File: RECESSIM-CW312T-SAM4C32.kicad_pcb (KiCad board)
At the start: 2 copper layers, 58.7 x 48.7 mm, 33 parts, among them U1 ATSAM4C32C

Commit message: Added two necessary resistors and removed one unnecessary one
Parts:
- added R6: 100k, Resistor_SMD:R_0603_1608Metric, F.Cu at (142.5, 102.2)
- R1: value 10k -> 100k
- moved R1 6.11 mm to (142.5, 104.2)
- moved R3 3.50 mm to (158.5, 89.3)
- moved TP2 3.20 mm to (143.8, 116.0)
- moved TP7 3.20 mm to (146.0, 116.0)
- moved R5 1.68 mm to (173.2, 109.8)
- moved C8 1.50 mm to (151.8, 116.8)
- moved C9 1.50 mm to (151.8, 118.5)
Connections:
- R1 pad 1: GND -> VCC
- R1 pad 2: Net-(JP1-C) -> Net-(U1-WKUP0/TMP0)

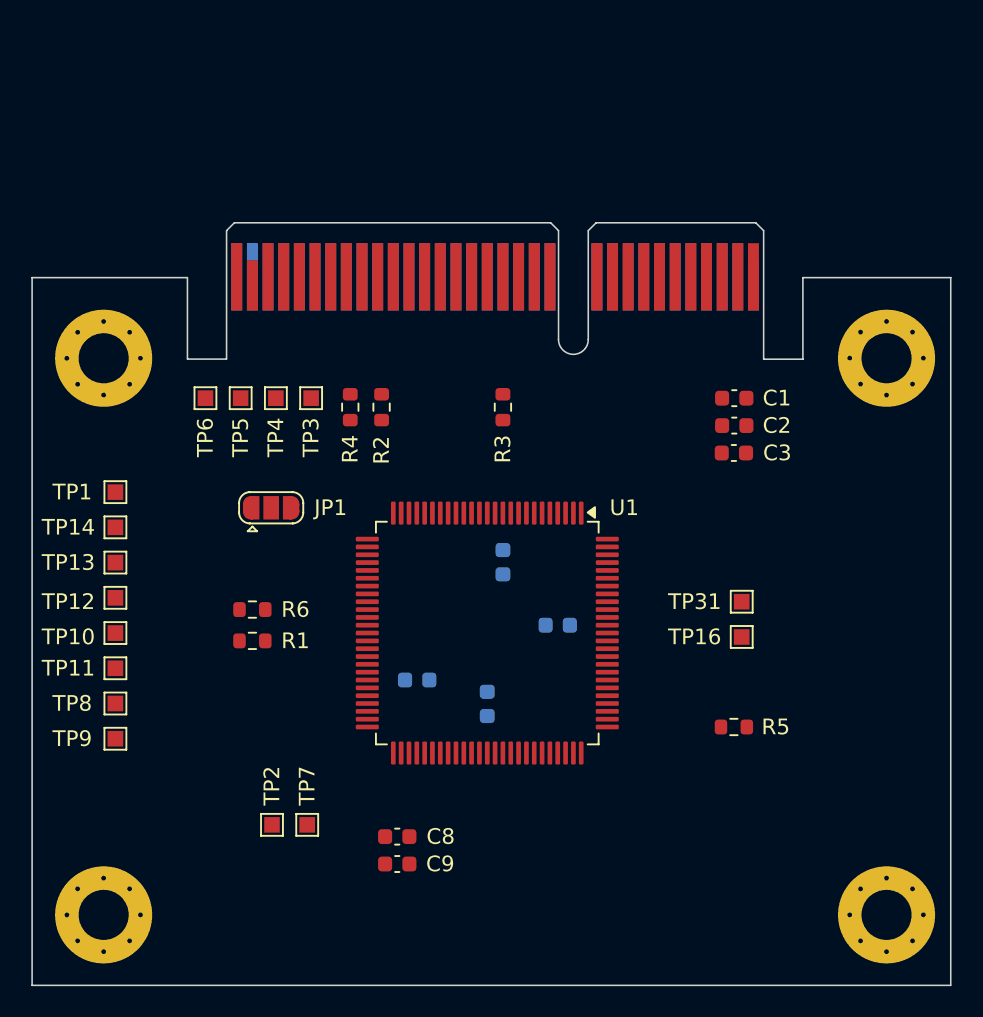
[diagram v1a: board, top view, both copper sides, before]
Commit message: Finalized PCB design, generated gerbers for version 1
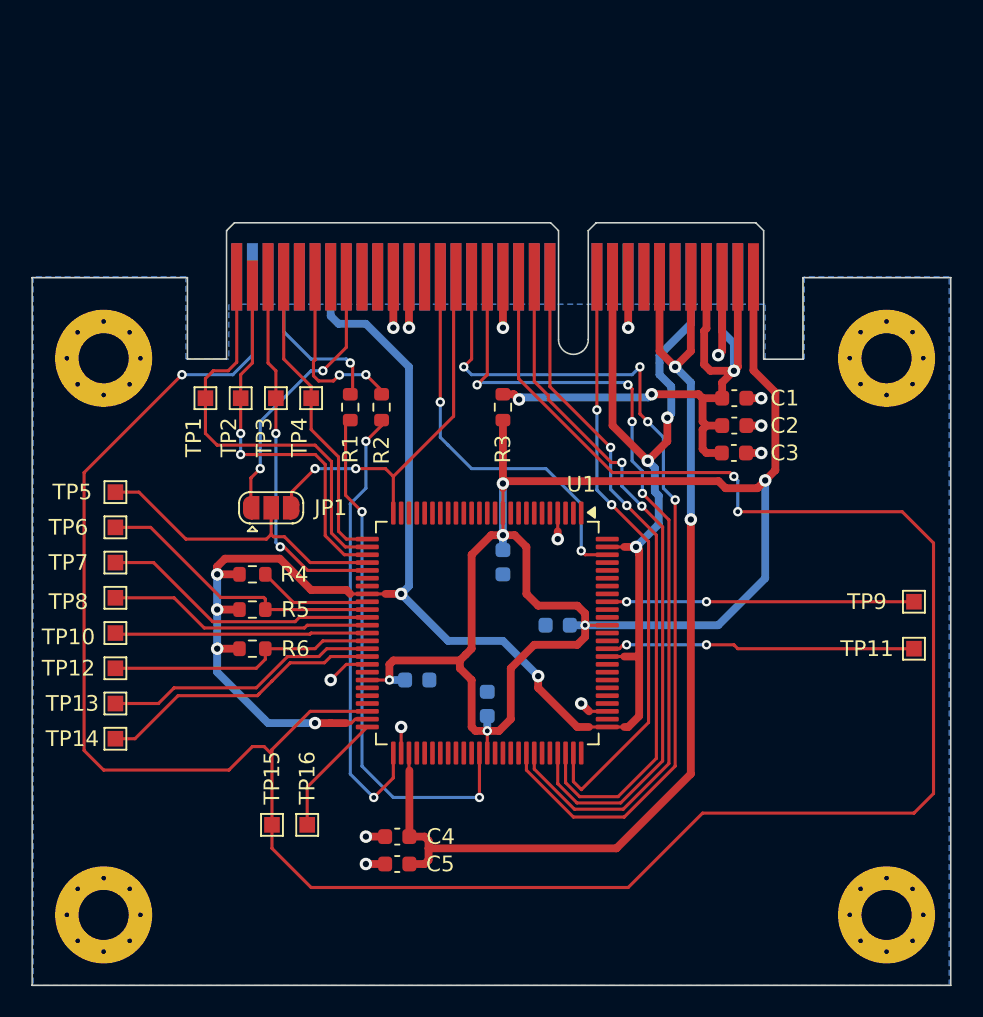
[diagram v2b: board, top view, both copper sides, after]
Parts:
- moved R4 32.3 mm to (142.5, 100.0)
- moved TP11 11.0 mm to (184.8, 104.8)
- moved TP9 11.0 mm to (184.8, 101.8)
- moved R6 0.50 mm to (142.5, 104.8)
- renumbered C8 to C4, C9 to C5, C4 to C6, C5 to C8, C6 to C9, R4 to R1, R5 to R4, R6 to R5, R1 to R6, TP6 to TP1, TP16 to TP11, TP11 to TP12, TP8 to TP13, TP9 to TP14, TP2 to TP15, TP7 to TP16, TP5 to TP2, TP4 to TP3, TP3 to TP4, TP1 to TP5, TP14 to TP6, TP13 to TP7, TP12 to TP8, TP31 to TP9
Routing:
- net /nRST: track 0.00 -> 163.7 mm, vias 0 -> 3
- net VCC: track 0.00 -> 125.3 mm, vias 0 -> 9
- net /SHUNTL: track 0.00 -> 111.0 mm, vias 0 -> 6
- net VCC1.2: track 0.00 -> 66.7 mm, vias 0 -> 2
- net /GPIO2_RX: track 0.00 -> 57.2 mm, vias 0 -> 4
- net /GPIO1_TX: track 0.00 -> 54.1 mm, vias 0 -> 4
- net /LED3: track 0.00 -> 45.0 mm, vias 0 -> 2
- net /LED2: track 0.00 -> 42.6 mm, vias 0 -> 2
- net /FILT_HP: track 0.00 -> 42.4 mm, vias 0 -> 3
- net /LED1: track 0.00 -> 38.4 mm, vias 0 -> 2
- net Net-(U1-PA6/PGMNOE): track 0.00 -> 33.8 mm, vias 0 -> 2
- net GND: track 0.00 -> 31.4 mm, vias 0 -> 14
- net Net-(U1-PA31/XIN): track 0.00 -> 28.9 mm, vias 0 -> 2
- net /JTAG_TCK: track 0.00 -> 27.4 mm
- net /GPIO4: track 0.00 -> 25.8 mm, vias 0 -> 2
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- added copper zone on B.Cu, net GND

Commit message: Finalized Rev1 of the PCB design, removed unused Test Points from Schematic
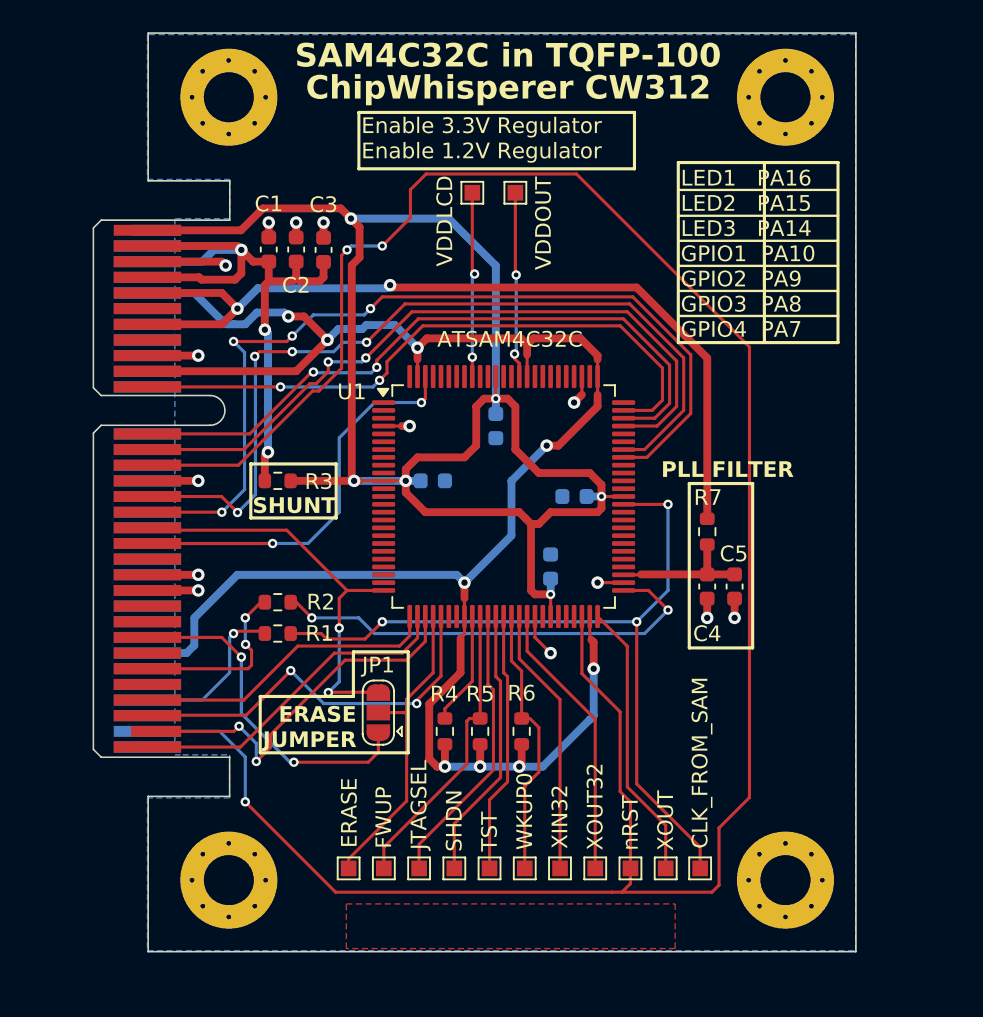
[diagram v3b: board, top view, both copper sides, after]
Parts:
- removed TP1, TP2, TP3, TP4: TestPoint, TestPoint:TestPoint_Pad_1.0x1.0mm
- added R7: 100, Resistor_SMD:R_0603_1608Metric, F.Cu at (171.6, 97.3)
- added TP22: CLK_FROM_SAM, TestPoint:TestPoint_Pad_1.0x1.0mm, F.Cu at (171.1, 118.8)
- TP10: value TestPoint -> TST
- TP11: value TestPoint -> VDDOUT
- TP12: value TestPoint -> WKUP0
- TP13: value TestPoint -> XIN32
- TP14: value TestPoint -> XOUT32
- TP15: value TestPoint -> nRST
- TP16: value TestPoint -> XOUT
- TP5: value TestPoint -> ERASE
- TP6: value TestPoint -> FWUP
- TP7: value TestPoint -> JTAGSEL
- TP8: value TestPoint -> SHDN
- TP9: value TestPoint -> VDDLCD
- moved P1 41.5 mm to (132.8, 119.5), turned to 90 degrees
- moved TP11 38.7 mm to (159.3, 75.6), turned to 90 degrees
- moved TP9 38.4 mm to (156.5, 75.6), turned to 90 degrees
- moved TP14 31.7 mm to (164.4, 118.8), turned to 90 degrees
- moved C1 31.2 mm to (143.5, 79.3), turned to 90 degrees
- moved TP13 30.3 mm to (162.1, 118.8), turned to 90 degrees
- moved C2 30.2 mm to (145.3, 79.3), turned to 90 degrees
- moved C3 29.2 mm to (147.0, 79.3), turned to 90 degrees
- moved TP12 29.1 mm to (159.9, 118.8), turned to 90 degrees
- moved TP5 28.3 mm to (148.6, 118.8), turned to 90 degrees
- moved TP10 28.2 mm to (157.6, 118.8), turned to 90 degrees
- moved C5 27.9 mm to (173.3, 100.8), turned to -90 degrees
- moved TP6 27.7 mm to (150.9, 118.8), turned to 90 degrees
- moved TP8 27.7 mm to (155.4, 118.8), turned to 90 degrees
- moved TP7 27.5 mm to (153.1, 118.8), turned to 90 degrees
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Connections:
- C4 pad 1: VCC1.2 -> Net-(U1-VDDPLL)
- C5 pad 1: VCC1.2 -> Net-(U1-VDDPLL)
- U1 pad 1: Net-(U1-PB6) -> unconnected-(U1-PB6-Pad1)
- U1 pad 10: Net-(U1-PB24) -> unconnected-(U1-PB24-Pad10)
- U1 pad 100: Net-(U1-PA2) -> unconnected-(U1-PA2-Pad100)
- U1 pad 12: Net-(U1-PB29) -> unconnected-(U1-PB29-Pad12)
- U1 pad 13: Net-(U1-PB9) -> unconnected-(U1-PB9-Pad13)
- U1 pad 14: Net-(U1-PB10) -> unconnected-(U1-PB10-Pad14)
- U1 pad 15: Net-(U1-PB11) -> unconnected-(U1-PB11-Pad15)
- U1 pad 16: Net-(U1-PB12) -> unconnected-(U1-PB12-Pad16)
- U1 pad 17: Net-(U1-PB14) -> unconnected-(U1-PB14-Pad17)
- U1 pad 18: Net-(U1-PB15) -> unconnected-(U1-PB15-Pad18)
- U1 pad 19: Net-(U1-PA26/PGMD14) -> unconnected-(U1-PA26/PGMD14-Pad19)
- U1 pad 2: Net-(U1-PB7) -> unconnected-(U1-PB7-Pad2)
- U1 pad 20: Net-(U1-PA25/PGMD13) -> unconnected-(U1-PA25/PGMD13-Pad20)
- U1 pad 21: Net-(U1-PA24/PGMD12) -> unconnected-(U1-PA24/PGMD12-Pad21)
- U1 pad 22: Net-(U1-PA20/PGMD8) -> unconnected-(U1-PA20/PGMD8-Pad22)
- U1 pad 23: Net-(U1-PA19/PGMD7) -> unconnected-(U1-PA19/PGMD7-Pad23)
- U1 pad 24: Net-(U1-PA18/PGMD6) -> unconnected-(U1-PA18/PGMD6-Pad24)
- U1 pad 3: Net-(U1-PB18) -> unconnected-(U1-PB18-Pad3)
- U1 pad 31: Net-(U1-PC1) -> unconnected-(U1-PC1-Pad31)
- U1 pad 32: Net-(U1-PC6) -> unconnected-(U1-PC6-Pad32)
- U1 pad 43: Net-(U1-PB4) -> unconnected-(U1-PB4-Pad43)
- U1 pad 45: Net-(U1-PB5) -> unconnected-(U1-PB5-Pad45)
- U1 pad 46: Net-(U1-PC7) -> unconnected-(U1-PC7-Pad46)
- U1 pad 47: Net-(U1-PC0) -> unconnected-(U1-PC0-Pad47)
- U1 pad 5: Net-(U1-PB19) -> unconnected-(U1-PB19-Pad5)
- U1 pad 53: VCC1.2 -> Net-(U1-VDDPLL)
- U1 pad 54: Net-(U1-PC8) -> unconnected-(U1-PC8-Pad54)
- U1 pad 55: Net-(U1-PC5) -> unconnected-(U1-PC5-Pad55)
- U1 pad 56: Net-(U1-PC4) -> unconnected-(U1-PC4-Pad56)
- U1 pad 57: Net-(U1-PC3) -> unconnected-(U1-PC3-Pad57)
- U1 pad 58: Net-(U1-PC2) -> unconnected-(U1-PC2-Pad58)
- U1 pad 59: Net-(U1-PA29) -> unconnected-(U1-PA29-Pad59)
- U1 pad 6: Net-(U1-PB8) -> unconnected-(U1-PB8-Pad6)
- U1 pad 60: Net-(U1-PA28) -> unconnected-(U1-PA28-Pad60)
- U1 pad 61: Net-(U1-PA27/PGMD15) -> unconnected-(U1-PA27/PGMD15-Pad61)
- U1 pad 64: Net-(U1-PA3) -> unconnected-(U1-PA3-Pad64)
- U1 pad 65: Net-(U1-PA21/PGMD9) -> unconnected-(U1-PA21/PGMD9-Pad65)
- U1 pad 66: Net-(U1-PA22/PGMD10) -> unconnected-(U1-PA22/PGMD10-Pad66)
- U1 pad 67: Net-(U1-PA23/PGMD11) -> unconnected-(U1-PA23/PGMD11-Pad67)
- U1 pad 7: Net-(U1-PB22) -> unconnected-(U1-PB22-Pad7)
- U1 pad 70: Net-(U1-PA11/PGMM3) -> unconnected-(U1-PA11/PGMM3-Pad70)
- U1 pad 71: Net-(U1-PA13/PGMD1) -> unconnected-(U1-PA13/PGMD1-Pad71)
- U1 pad 75: Net-(U1-PA17/PGMD5) -> unconnected-(U1-PA17/PGMD5-Pad75)
- U1 pad 77: Net-(U1-ADVREF) -> unconnected-(U1-ADVREF-Pad77)
- U1 pad 79: Net-(U1-PB31/AD5) -> unconnected-(U1-PB31/AD5-Pad79)
- U1 pad 8: Net-(U1-PB30) -> unconnected-(U1-PB30-Pad8)
- U1 pad 80: Net-(U1-PB23/AD4) -> unconnected-(U1-PB23/AD4-Pad80)
- U1 pad 81: Net-(U1-PB13/AD3) -> unconnected-(U1-PB13/AD3-Pad81)
- U1 pad 82: Net-(U1-PA5/AD2/PGMRDY) -> unconnected-(U1-PA5/AD2/PGMRDY-Pad82)
- U1 pad 83: Net-(U1-PA4/AD1/PGMNCMD) -> unconnected-(U1-PA4/AD1/PGMNCMD-Pad83)
- U1 pad 84: Net-(U1-PA12/AD0/PGMD0) -> unconnected-(U1-PA12/AD0/PGMD0-Pad84)
- U1 pad 87: Net-(U1-PB21) -> unconnected-(U1-PB21-Pad87)
- U1 pad 88: Net-(U1-PB20) -> unconnected-(U1-PB20-Pad88)
- U1 pad 9: Net-(U1-PB25) -> unconnected-(U1-PB25-Pad9)
- U1 pad 90: Net-(U1-PA0/PGMEN0) -> unconnected-(U1-PA0/PGMEN0-Pad90)
- U1 pad 91: Net-(U1-PB27/TMP2) -> unconnected-(U1-PB27/TMP2-Pad91)
- U1 pad 93: Net-(U1-PB26) -> unconnected-(U1-PB26-Pad93)
- U1 pad 94: Net-(U1-PB28/TMP3) -> unconnected-(U1-PB28/TMP3-Pad94)
- U1 pad 95: Net-(U1-PB16/TMP1) -> unconnected-(U1-PB16/TMP1-Pad95)
- U1 pad 96: Net-(U1-PA1/PGMEN1) -> unconnected-(U1-PA1/PGMEN1-Pad96)
- U1 pad 97: Net-(U1-PB17) -> unconnected-(U1-PB17-Pad97)
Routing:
- net Net-(U1-PA6/PGMNOE): track 33.8 -> 51.3 mm, vias 2 -> 3
- net VCC1.2: track 66.7 -> 55.1 mm
- net /nRST: track 163.7 -> 152.9 mm
- net Net-(U1-PA30/XOUT): track 7.84 -> 17.9 mm
- net Net-(U1-VDDPLL): track 0.00 -> 8.97 mm
- net Net-(U1-VDDOUT): track 19.8 -> 11.9 mm
- net Net-(U1-VDDLCD): track 19.6 -> 11.9 mm
- net /JTAG_TCK: track 27.4 -> 21.5 mm
- net /BOOT_MODE: track 17.7 -> 21.7 mm
- net /LED1: track 38.4 -> 40.9 mm
- net /GPIO3: track 25.1 -> 27.0 mm
- net /JTAG_TDO: track 23.8 -> 25.5 mm
- net /LED2: track 42.6 -> 43.7 mm
- net /GPIO1_TX: track 54.1 -> 55.1 mm
- net /LED3: track 45.0 -> 45.9 mm
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- added copper zone on F.Cu, net (none)
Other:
- board size 58.7 x 48.7 mm -> 48.7 x 58.7 mm
- board text added: "CVEs are for SNITCHES"
- board text added: "ChipWhisperer CW312"
- board text added: "ERASE JUMPER"
- board text added: "Enable 3.3V Regulator Enable 1.2V Regulator"
- board text added: "LED1 PA16 LED2 PA15 LED3 PA14 GPIO1 PA10 GPIO2 PA9 GPIO3 PA8 GPIO4 PA7"
- board text added: "PLL FILTER"
- board text added: "RECESSIM"
- board text added: "Rev.1"
- board text added: "SAM4C32C in TQFP-100"
- board text added: "SHUNT"

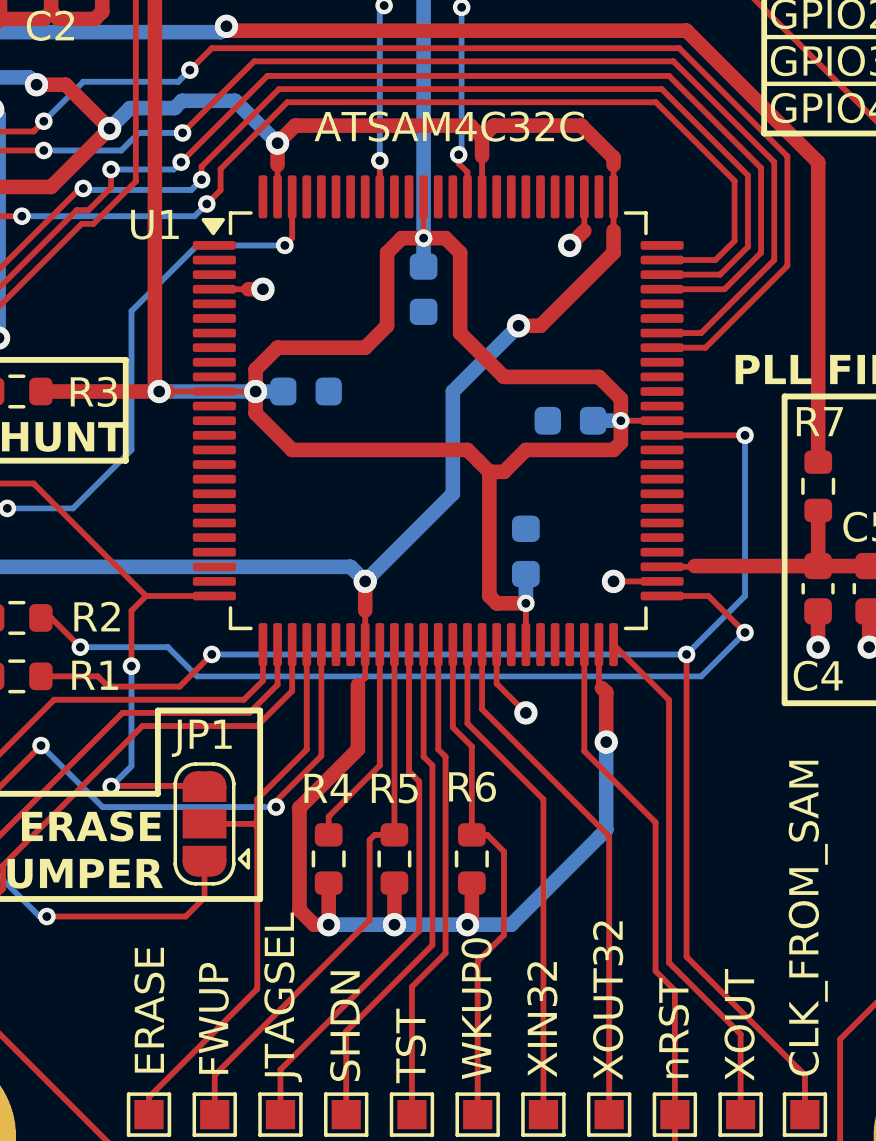
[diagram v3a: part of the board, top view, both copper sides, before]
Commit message: Changed processor footprint to have pad spacing of 0.22mm so black solder mask will bridge.
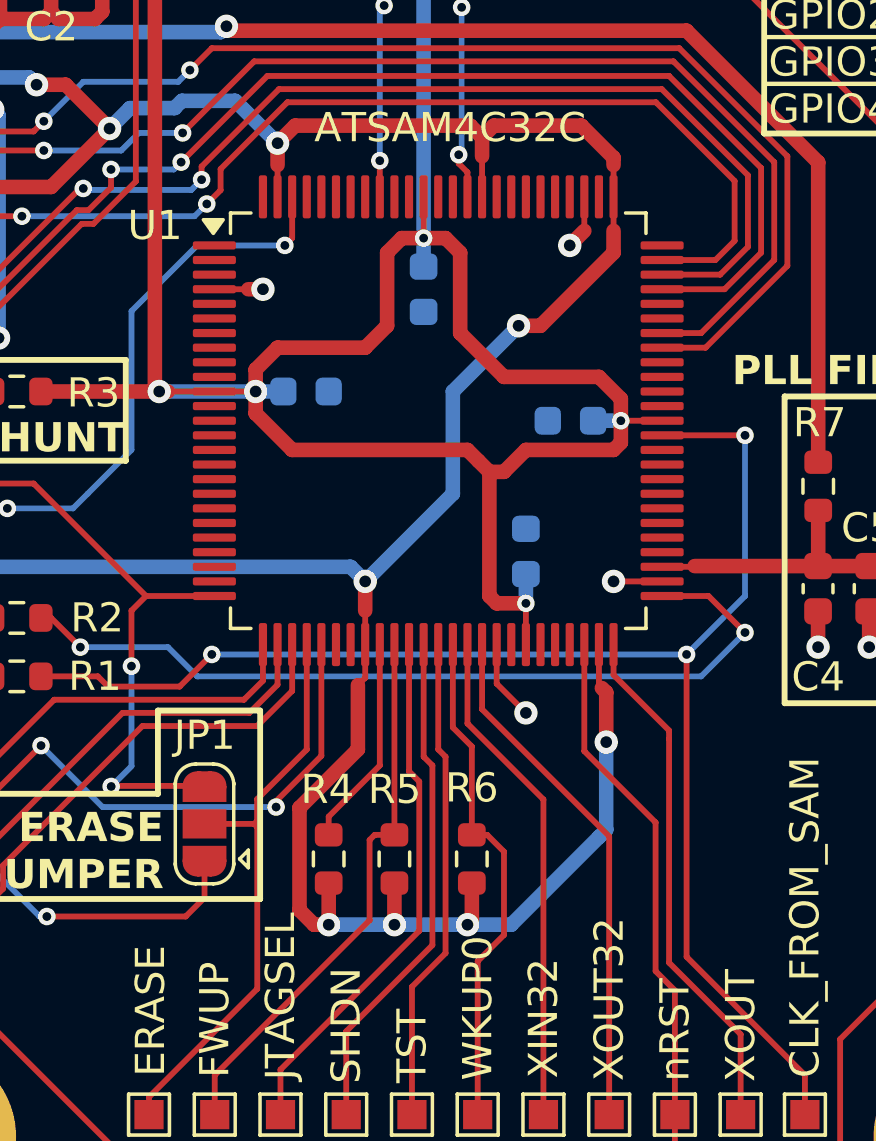
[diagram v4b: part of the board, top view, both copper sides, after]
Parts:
- U1: footprint Package_QFP:TQFP-100_14x14mm_P0.5mm -> RECESSIM-CW312T-SAM4C32:TQFP-100_14x14mm_P0.5mm_W0.28mm

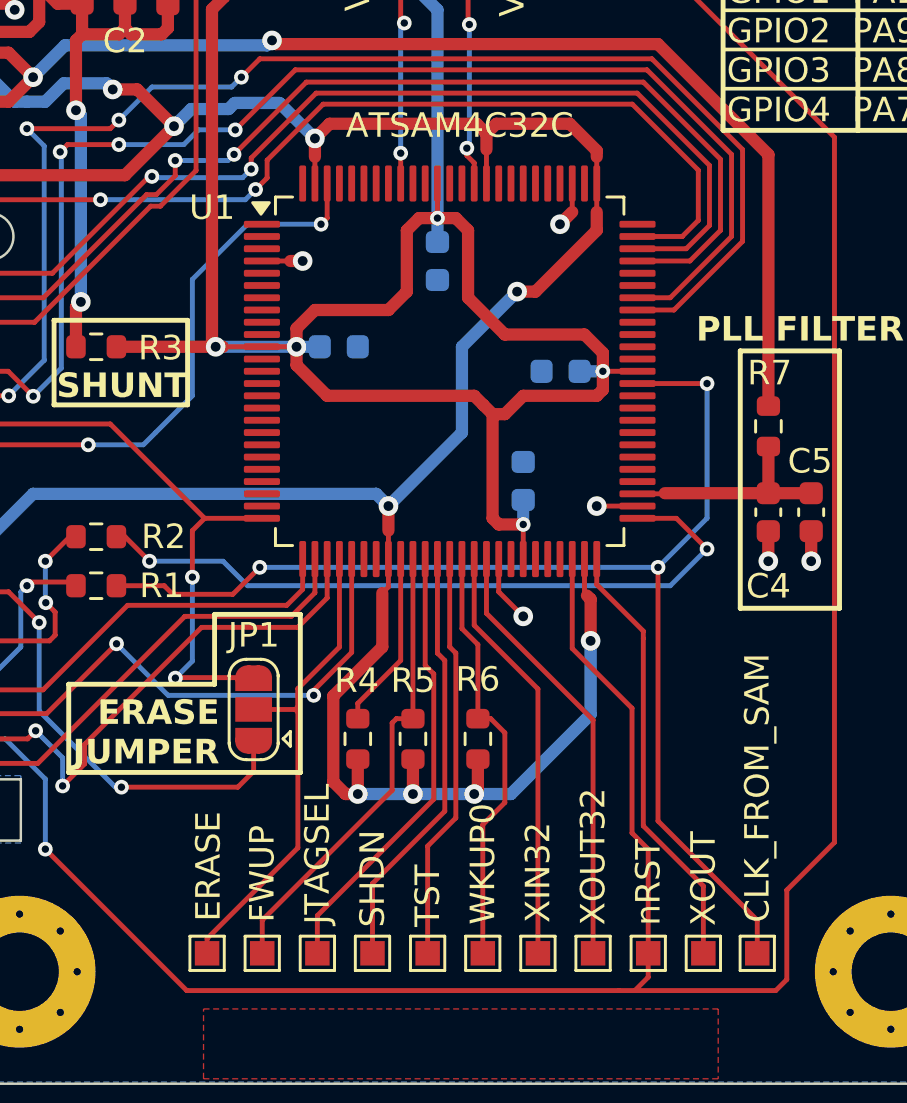
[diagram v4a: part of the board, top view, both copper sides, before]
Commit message: Fixed TX/RX UART pin locations, updated PCB and regenerated gerbers
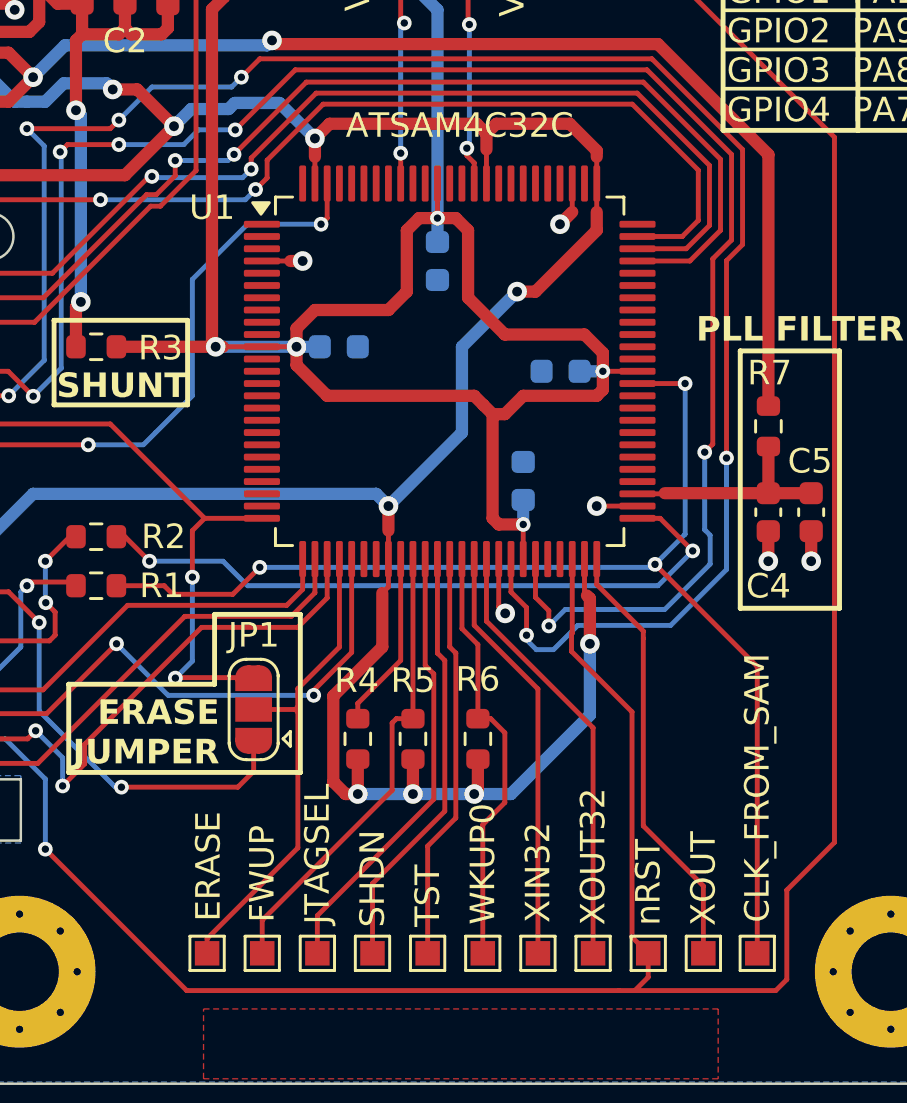
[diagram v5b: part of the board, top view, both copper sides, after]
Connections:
- U1 pad 43: unconnected-(U1-PB4-Pad43) -> /GPIO2_RX
- U1 pad 45: unconnected-(U1-PB5-Pad45) -> /GPIO1_TX
- U1 pad 68: /GPIO2_RX -> unconnected-(U1-PA9/PGMM1-Pad68)
- U1 pad 69: /GPIO1_TX -> unconnected-(U1-PA10/PGMM2-Pad69)
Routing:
- net /GPIO2_RX: track 57.7 -> 79.2 mm, vias 4 -> 6
- net /GPIO1_TX: track 55.1 -> 74.7 mm, vias 4 -> 6
- net Net-(U1-PA6/PGMNOE): track 51.3 -> 50.1 mm
- net Net-(U1-PA31/XIN): track 28.9 -> 27.7 mm
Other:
- board text added: "Rev.2"
- board text removed: "Rev.1"
